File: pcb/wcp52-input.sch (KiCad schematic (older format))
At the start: 18 parts, among them J1 5V, J2 -5V, J3 IN1, J4 IN2, J5 CTRL, J6 PHASEREF, J7 5V, Q1 PMV160UP, Q2 2N7002

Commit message: Routed PCB
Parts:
- removed C1: 47u, IPC7351-Nominal:CAPC3216X70, symbol C-1206
- removed J1: 5V, conn:CONN_2-SIL, symbol HEAD-F2
- removed J2: -5V, conn:CONN_2-SIL, symbol HEAD-F2
- added J1: 5V, conn:CONN_3-SIL, symbol HEAD-M3
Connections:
- net GND: now also J1.2
- net at Q1.3: now also J1.1
- net at Q2.3: now also J1.3
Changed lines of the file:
@@
-$EndComp
-$Comp
-L HEAD-F2 J1
-U 1 1 54566388
-P 800 2000
-F 0 "J1" H 800 2200 50  0000 C CNN
-F 1 "5V" H 800 2100 50  0000 C CNN
-F 2 "conn:CONN_2-SIL" H 800 2000 50  0001 C CNN
-F 3 "" H 800 2000 50  0000 C CNN
-	1    800  2000
-	-1   0    0    -1
-$EndComp
-$Comp
-L GND #PWR01
-U 1 1 54566416
-P 950 2150
-F 0 "#PWR01" H 950 2150 30  0001 C CNN
-F 1 "GND" H 950 2080 30  0001 C CNN
-F 2 "" H 950 2150 60  0000 C CNN
-F 3 "" H 950 2150 60  0000 C CNN
-	1    950  2150
-	1    0    0    -1
 $EndComp
 $Comp
@@
 $EndComp
 $Comp
-L GND #PWR02
+L GND #PWR01
 U 1 1 545666B4
 P 1350 2150
-F 0 "#PWR02" H 1350 2150 30  0001 C CNN
+F 0 "#PWR01" H 1350 2150 30  0001 C CNN
 F 1 "GND" H 1350 2080 30  0001 C CNN
 F 2 "" H 1350 2150 60  0000 C CNN
@@
 $EndComp
 $Comp
-L GND #PWR03
+L GND #PWR02
 U 1 1 545670CB
 P 9950 3750
-F 0 "#PWR03" H 9950 3750 30  0001 C CNN
+F 0 "#PWR02" H 9950 3750 30  0001 C CNN
 F 1 "GND" H 9950 3680 30  0001 C CNN
 F 2 "" H 9950 3750 60  0000 C CNN
@@
 $EndComp
 $Comp
-L GND #PWR04
+L GND #PWR03
 U 1 1 54568BA2
 P 9400 4000
-F 0 "#PWR04" H 9400 4000 30  0001 C CNN
+F 0 "#PWR03" H 9400 4000 30  0001 C CNN
 F 1 "GND" H 9400 3930 30  0001 C CNN
 F 2 "" H 9400 4000 60  0000 C CNN
@@
 $EndComp
 $Comp
-L GND #PWR05
+L GND #PWR04
 U 1 1 54568DC5
 P 8800 4000
-F 0 "#PWR05" H 8800 4000 30  0001 C CNN
+F 0 "#PWR04" H 8800 4000 30  0001 C CNN
 F 1 "GND" H 8800 3930 30  0001 C CNN
 F 2 "" H 8800 4000 60  0000 C CNN
@@
 $EndComp
 $Comp
-L GND #PWR06
+L GND #PWR05
 U 1 1 5456956E
 P 2350 4900
-F 0 "#PWR06" H 2350 4900 30  0001 C CNN
+F 0 "#PWR05" H 2350 4900 30  0001 C CNN
 F 1 "GND" H 2350 4830 30  0001 C CNN
 F 2 "" H 2350 4900 60  0000 C CNN
@@
 $EndComp
 $Comp
-L HEAD-F2 J2
-U 1 1 5456E715
-P 800 2650
-F 0 "J2" H 800 2850 50  0000 C CNN
-F 1 "-5V" H 800 2750 50  0000 C CNN
-F 2 "conn:CONN_2-SIL" H 800 2650 50  0001 C CNN
-F 3 "" H 800 2650 50  0000 C CNN
-	1    800  2650
-	-1   0    0    -1
-$EndComp
-$Comp
-L GND #PWR07
-U 1 1 5456EA8D
-P 950 2850
-F 0 "#PWR07" H 950 2850 30  0001 C CNN
-F 1 "GND" H 950 2780 30  0001 C CNN
-F 2 "" H 950 2850 60  0000 C CNN
-F 3 "" H 950 2850 60  0000 C CNN
-	1    950  2850
-	1    0    0    -1
-$EndComp
-$Comp
-L GND #PWR08
+L GND #PWR06
 U 1 1 5456EDD5
 P 1350 2850
-F 0 "#PWR08" H 1350 2850 30  0001 C CNN
+F 0 "#PWR06" H 1350 2850 30  0001 C CNN
 F 1 "GND" H 1350 2780 30  0001 C CNN
 F 2 "" H 1350 2850 60  0000 C CNN
@@
 $EndComp
 $Comp
-L GND #PWR09
+L GND #PWR07
 U 1 1 5456F3BD
 P 2500 3000
-F 0 "#PWR09" H 2500 3000 30  0001 C CNN
+F 0 "#PWR07" H 2500 3000 30  0001 C CNN
 F 1 "GND" H 2500 2930 30  0001 C CNN
 F 2 "" H 2500 3000 60  0000 C CNN
@@
 $EndComp
 $Comp
-L -5 #PWR010
+L -5 #PWR08
 U 1 1 5456F4D5
 P 2500 2600
-F 0 "#PWR010" H 2500 2550 30  0001 C CNN
+F 0 "#PWR08" H 2500 2550 30  0001 C CNN
 F 1 "-5" H 2500 2500 50  0000 C CNN
 F 2 "" H 2500 2600 60  0000 C CNN
@@
 $EndSheet
 $Comp
-L GND #PWR011
+L GND #PWR09
 U 1 1 545F0319
 P 800 3950
-F 0 "#PWR011" H 800 3950 30  0001 C CNN
+F 0 "#PWR09" H 800 3950 30  0001 C CNN
 F 1 "GND" H 800 3880 30  0001 C CNN
 F 2 "" H 800 3950 60  0000 C CNN
@@
 $EndComp
 $Comp
-L GND #PWR012
+L GND #PWR010
 U 1 1 545F03CC
 P 800 3450
-F 0 "#PWR012" H 800 3450 30  0001 C CNN
+F 0 "#PWR010" H 800 3450 30  0001 C CNN
 F 1 "GND" H 800 3380 30  0001 C CNN
 F 2 "" H 800 3450 60  0000 C CNN
@@
 $EndComp
 $Comp
-L GND #PWR013
+L GND #PWR011
 U 1 1 545F0F87
 P 950 5550
-F 0 "#PWR013" H 950 5550 30  0001 C CNN
+F 0 "#PWR011" H 950 5550 30  0001 C CNN
 F 1 "GND" H 950 5480 30  0001 C CNN
 F 2 "" H 950 5550 60  0000 C CNN
@@
 $EndComp
 $Comp
-L GND #PWR014
+L GND #PWR012
 U 1 1 545F19A6
 P 800 6050
-F 0 "#PWR014" H 800 6050 30  0001 C CNN
+F 0 "#PWR012" H 800 6050 30  0001 C CNN
 F 1 "GND" H 800 5980 30  0001 C CNN
 F 2 "" H 800 6050 60  0000 C CNN
@@
 	1    0    0    -1
 $EndComp
-Wire Wire Line
-	950  2150 950  2100
-Wire Wire Line
-	950  2100 850  2100
 Wire Wire Line
 	1250 2000 850  2000
@@
 	2350 4900 2350 4850
 Wire Wire Line
-	950  2850 950  2750
-Wire Wire Line
-	950  2750 850  2750
-Wire Wire Line
 	1250 2650 850  2650
 Wire Wire Line
@@
 Wire Wire Line
 	2000 2000 2500 2000
-Wire Wire Line
-	2500 1900 2500 2100
-$Comp
-L +5 #PWR015
+$Comp
+L +5 #PWR013
 U 1 1 545F34F4
 P 2500 1900
-F 0 "#PWR015" H 2500 1950 30  0001 C CNN
+F 0 "#PWR013" H 2500 1950 30  0001 C CNN
 F 1 "+5" H 2500 2000 50  0000 C CNN
 F 2 "" H 2500 1900 60  0000 C CNN
@@
 	1    0    0    -1
 $EndComp
-$Comp
-L C-1206 C1
-U 1 1 545F3E9C
-P 2500 2200
-F 0 "C1" H 2750 2250 50  0000 C CNN
-F 1 "47u" H 2750 2150 50  0000 C CNN
-F 2 "IPC7351-Nominal:CAPC3216X70" H 2490 2175 60  0001 C CNN
-F 3 "" H 2490 2175 60  0000 C CNN
-F 4 "GRM31CR61A476ME15L" H 1950 2150 40  0000 C CNN "PN"
-F 5 "Murata" H 1950 2250 40  0000 C CNN "Manuf"
-	1    2500 2200
-	-1   0    0    -1
-$EndComp
-Connection ~ 2500 2000
-$Comp
-L GND #PWR016
-U 1 1 545F4038
-P 2500 2350
-F 0 "#PWR016" H 2500 2350 30  0001 C CNN
-F 1 "GND" H 2500 2280 30  0001 C CNN
-F 2 "" H 2500 2350 60  0000 C CNN
-F 3 "" H 2500 2350 60  0000 C CNN
-	1    2500 2350
-	1    0    0    -1
-$EndComp
-Wire Wire Line
-	2500 2350 2500 2300
 Wire Wire Line
 	7000 3550 6750 3550
@@
 	1    0    0    1
 $EndComp
+Wire Wire Line
+	2500 2000 2500 1900
+$Comp
+L HEAD-M3 J1
+U 1 1 545FFD0F
+P 700 2200
+F 0 "J1" H 700 2400 50  0000 C CNN
+F 1 "5V" H 700 2300 50  0000 C CNN
+F 2 "conn:CONN_3-SIL" H 700 2200 50  0001 C CNN
+F 3 "" H 700 2200 50  0000 C CNN
+	1    700  2200
+	-1   0    0    -1
+$EndComp
+Wire Wire Line
+	750  2200 850  2200
+Wire Wire Line
+	850  2200 850  2000
+Wire Wire Line
+	750  2400 850  2400
+Wire Wire Line
+	850  2400 850  2650
+$Comp
+L GND #PWR014
+U 1 1 5460014A
+P 1000 2300
+F 0 "#PWR014" H 1000 2300 30  0001 C CNN
+F 1 "GND" H 1000 2230 30  0001 C CNN
+F 2 "" H 1000 2300 60  0000 C CNN
+F 3 "" H 1000 2300 60  0000 C CNN
+	1    1000 2300
+	0    -1   -1   0
+$EndComp
+Wire Wire Line
+	750  2300 1000 2300
 $EndSCHEMATC

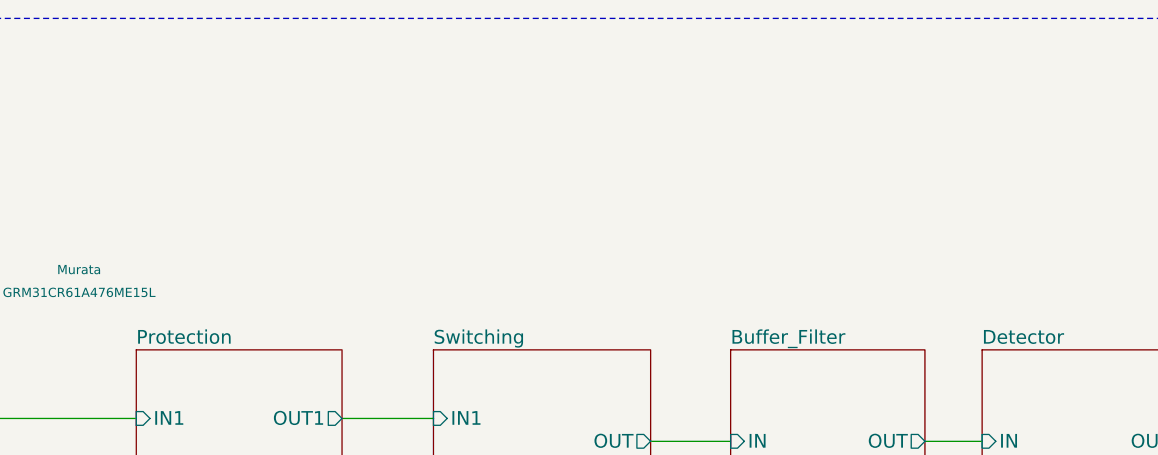
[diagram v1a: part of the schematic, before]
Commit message: Added more decoupling
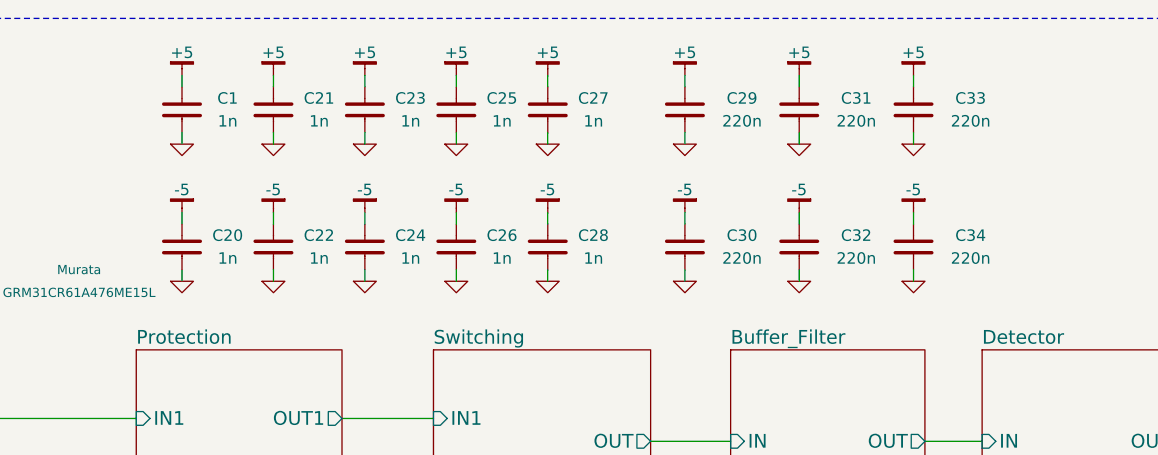
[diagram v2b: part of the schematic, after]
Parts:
- added C1, C20, C21, C22, C23, C24, C25, C26, C27, C28: 1n, IPC7351-Nominal:CAPC1005X55, symbol C-0402
- added C29, C30, C31, C32, C33, C34: 220n, IPC7351-Nominal:CAPC2012X70, symbol C-0805
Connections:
- net +5: now also C1.1, C21.1, C23.1, C25.1, C27.1, C29.1, C31.1, C33.1
- net -5: now also C20.1, C22.1, C24.1, C26.1, C28.1, C30.1, C32.1, C34.1
- net GND: now also C1.2, C20.2, C21.2, C22.2, C23.2, C24.2, C25.2, C26.2, C27.2, C28.2, C29.2, C30.2, C31.2, C32.2, C33.2, C34.2

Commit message: Switched to PTH SMA connectors
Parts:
- J3, J4, J6: footprint conn:CONN-2_CONSMA001-SMD-G -> conn:CONN-2_CONSMA001
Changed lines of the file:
@@
 F 0 "J4" H 800 4000 50  0000 C CNN
 F 1 "IN2" H 800 3900 50  0000 C CNN
-F 2 "conn:CONN-2_CONSMA001-SMD-G" H 800 3800 50  0001 C CNN
+F 2 "conn:CONN-2_CONSMA001" H 800 3800 50  0001 C CNN
 F 3 "" H 800 3800 50  0000 C CNN
 	1    800  3800
@@
 F 0 "J3" H 800 3500 50  0000 C CNN
 F 1 "IN1" H 800 3400 50  0000 C CNN
-F 2 "conn:CONN-2_CONSMA001-SMD-G" H 800 3300 50  0001 C CNN
+F 2 "conn:CONN-2_CONSMA001" H 800 3300 50  0001 C CNN
 F 3 "" H 800 3300 50  0000 C CNN
 	1    800  3300
@@
 F 0 "J6" H 800 6100 50  0000 C CNN
 F 1 "PHASEREF" H 800 6000 50  0000 C CNN
-F 2 "conn:CONN-2_CONSMA001-SMD-G" H 800 5900 50  0001 C CNN
+F 2 "conn:CONN-2_CONSMA001" H 800 5900 50  0001 C CNN
 F 3 "" H 800 5900 50  0000 C CNN
 	1    800  5900

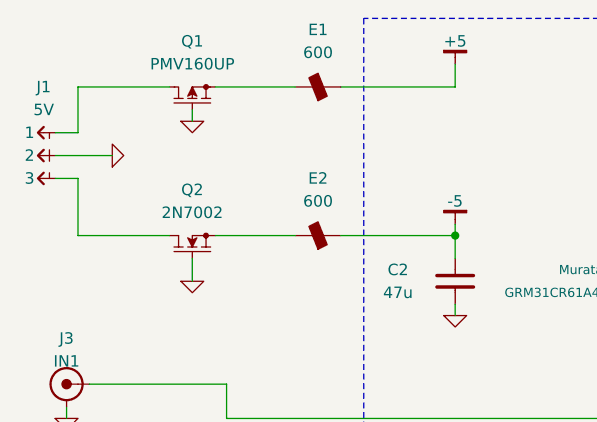
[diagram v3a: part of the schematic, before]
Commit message: Updated MOSFET types
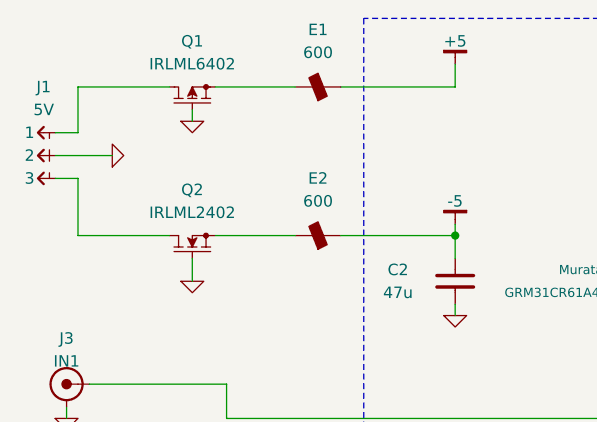
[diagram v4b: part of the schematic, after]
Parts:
- Q1: value PMV160UP -> IRLML6402
- Q2: value 2N7002 -> IRLML2402
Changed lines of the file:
@@
 EESchema Schematic File Version 2
-LIBS:1N
-LIBS:1N-SMD
-LIBS:2N
-LIBS:2N-SMD
-LIBS:4000
-LIBS:7400
-LIBS:ad
-LIBS:altera
 LIBS:atmel
-LIBS:capacitors
 LIBS:conn
-LIBS:diodesinc
 LIBS:display
-LIBS:electromech
-LIBS:fairchild_ic
-LIBS:fairchild_semi
 LIBS:ftdi
-LIBS:ic_template
-LIBS:inductors
-LIBS:infineon
-LIBS:intersil
-LIBS:irf
-LIBS:ixys
-LIBS:lattice
-LIBS:ltc
-LIBS:maxim
-LIBS:mechanical
 LIBS:microchip
-LIBS:nxp_ic
-LIBS:nxp_semi
-LIBS:onsemi
-LIBS:passive
 LIBS:power
-LIBS:resistors
-LIBS:russian-nixies
-LIBS:semi
-LIBS:silabs
-LIBS:skyworks
-LIBS:st_ic
-LIBS:st_semi
 LIBS:supertex
-LIBS:symbol
 LIBS:texas
-LIBS:vishay_semi
 LIBS:wcp52-input-cache
 EELAYER 25 0
@@
 P 1350 2050
 F 0 "Q1" V 1600 2050 50  0000 C CNN
-F 1 "PMV160UP" V 1500 2050 50  0000 C CNN
+F 1 "IRLML6402" V 1500 2050 50  0000 C CNN
 F 2 "IPC-semi-nominal:SOT-23" H 1350 2050 60  0001 C CNN
 F 3 "" H 1350 2050 60  0000 C CNN
@@
 P 1350 2700
 F 0 "Q2" V 1600 2700 50  0000 C CNN
-F 1 "2N7002" V 1500 2700 50  0000 C CNN
+F 1 "IRLML2402" V 1500 2700 50  0000 C CNN
 F 2 "IPC-semi-nominal:SOT-23" H 1350 2700 60  0001 C CNN
 F 3 "" H 1350 2700 60  0000 C CNN
